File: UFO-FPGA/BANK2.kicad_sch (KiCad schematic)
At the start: 11 parts, among them U1 ICE40HX8K-BG121

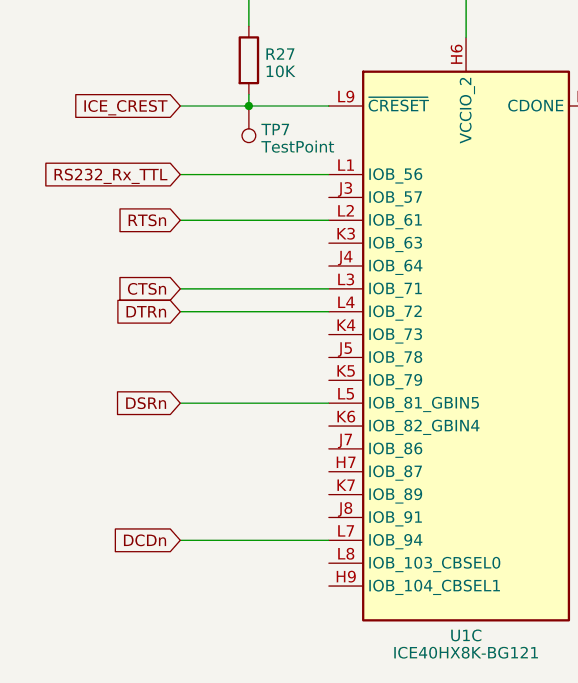
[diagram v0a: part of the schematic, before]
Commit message: Opamp gemaakt van de ADC
Enkel nog begrijpen wat VDC is. Aan docent vragen?
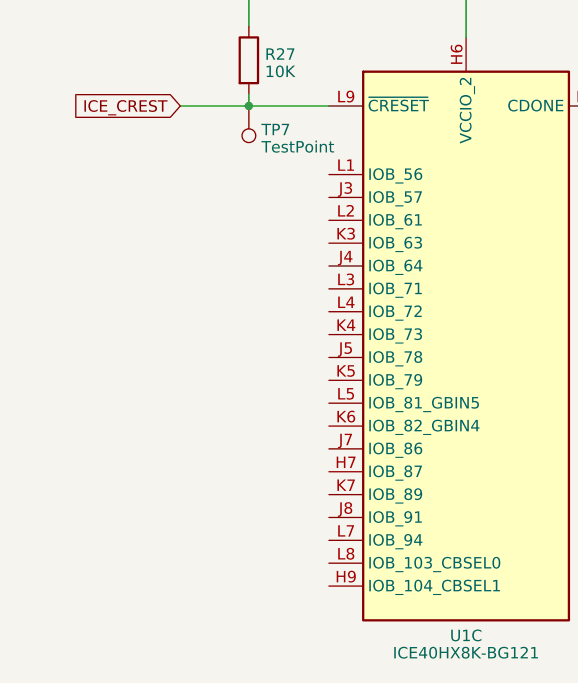
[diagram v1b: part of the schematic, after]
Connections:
- net CTSn: no longer names the net of U1.L3 (IOB_71)
- net DCDn: no longer names the net of U1.L7 (IOB_94)
- net DSRn: no longer names the net of U1.L5 (IOB_81_GBIN5)
- net DTRn: no longer names the net of U1.L4 (IOB_72)
- net RS232_Rx_TTL: no longer names the net of U1.L1 (IOB_56)
- net RTSn: no longer names the net of U1.L2 (IOB_61)
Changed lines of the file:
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@@
-    (stroke (width 0) (type default))
-  )
-  (wire (pts (xy 114.3 71.12) (xy 130.81 71.12))
     (stroke (width 0) (type default))
   )
@@
     (stroke (width 0) (type default))
   )
-  (wire (pts (xy 114.3 66.04) (xy 130.81 66.04))
-    (stroke (width 0) (type default))
-  )
-  (wire (pts (xy 114.3 106.68) (xy 130.81 106.68))
-    (stroke (width 0) (type default))
-  )
-  (wire (pts (xy 114.3 78.74) (xy 130.81 78.74))
-    (stroke (width 0) (type default))
-  )
   (wire (pts (xy 198.12 58.42) (xy 204.47 58.42))
-    (stroke (width 0) (type default))
-  )
-  (wire (pts (xy 114.3 91.44) (xy 130.81 91.44))
     (stroke (width 0) (type default))
   )
@@
   )
   (wire (pts (xy 146.05 38.1) (xy 146.05 50.8))
-    (stroke (width 0) (type default))
-  )
-  (wire (pts (xy 114.3 81.28) (xy 130.81 81.28))
     (stroke (width 0) (type default))
   )
@@
     (effects (font (size 1.27 1.27)) (justify left bottom))
   )
-  (global_label "RS232_Rx_TTL" (shape input) (at 114.3 66.04 180) (fields_autoplaced)
-    (effects (font (size 1.27 1.27)) (justify right))
-    (property "Intersheetrefs" "${INTERSHEET_REFS}" (at 98.0896 66.04 0)
-      (effects (font (size 1.27 1.27)) (justify right) hide)
-    )
-  )
-  (global_label "DTRn" (shape input) (at 114.3 81.28 180) (fields_autoplaced)
-    (effects (font (size 1.27 1.27)) (justify right))
-    (property "Intersheetrefs" "${INTERSHEET_REFS}" (at 106.7376 81.28 0)
-      (effects (font (size 1.27 1.27)) (justify right) hide)
-    )
-  )
   (global_label "ICE_CREST" (shape input) (at 114.3 58.42 180) (fields_autoplaced)
     (effects (font (size 1.27 1.27)) (justify right))
@@
       (effects (font (size 1.27 1.27)) (justify right) hide)
     )
-  )
-  (global_label "RTSn" (shape input) (at 114.3 71.12 180) (fields_autoplaced)
-    (effects (font (size 1.27 1.27)) (justify right))
-    (property "Intersheetrefs" "${INTERSHEET_REFS}" (at 106.7981 71.12 0)
-      (effects (font (size 1.27 1.27)) (justify right) hide)
-    )
-  )
-  (global_label "DSRn" (shape input) (at 114.3 91.44 180) (fields_autoplaced)
-    (effects (font (size 1.27 1.27)) (justify right))
-    (property "Intersheetrefs" "${INTERSHEET_REFS}" (at 106.4957 91.44 0)
-      (effects (font (size 1.27 1.27)) (justify right) hide)
-    )
-  )
-  (global_label "CTSn" (shape input) (at 114.3 78.74 180) (fields_autoplaced)
-    (effects (font (size 1.27 1.27)) (justify right))
-    (property "Intersheetrefs" "${INTERSHEET_REFS}" (at 106.7981 78.74 0)
-      (effects (font (size 1.27 1.27)) (justify right) hide)
-    )
-  )
-  (global_label "DCDn" (shape input) (at 114.3 106.68 180) (fields_autoplaced)
-    (effects (font (size 1.27 1.27)) (justify right))
-    (property "Intersheetrefs" "${INTERSHEET_REFS}" (at 106.4352 106.68 0)
-      (effects (font (size 1.27 1.27)) (justify right) hide)
-    )

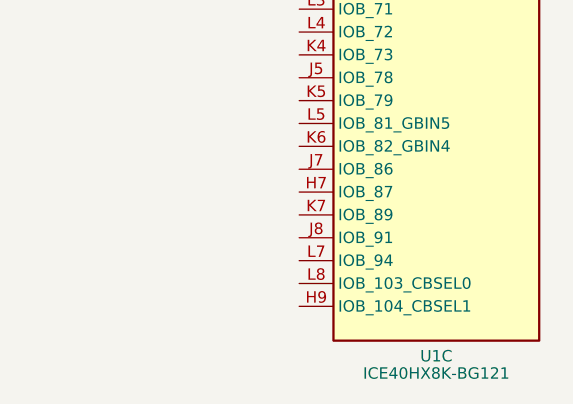
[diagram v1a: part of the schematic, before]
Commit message: Arduino PCB
Added Arduino PCB format
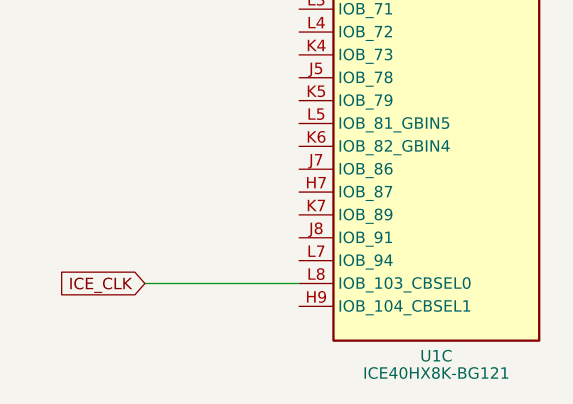
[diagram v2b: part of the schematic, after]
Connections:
- net ICE_CLK: now reaches U1.L8 (IOB_103_CBSEL0)
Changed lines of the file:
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@@
+    (stroke (width 0) (type default))
+  )
+  (wire (pts (xy 113.665 109.22) (xy 130.81 109.22))
     (stroke (width 0) (type default))
   )
@@
     (effects (font (size 1.27 1.27)) (justify left bottom))
   )
+  (global_label "ICE_CLK" (shape input) (at 113.665 109.22 180) (fields_autoplaced)
+    (effects (font (size 1.27 1.27)) (justify right))
+    (property "Intersheetrefs" "${INTERSHEET_REFS}" (at 103.1997 109.22 0)
+      (effects (font (size 1.27 1.27)) (justify right) hide)
+    )
+  )
   (global_label "ICE_CREST" (shape input) (at 114.3 58.42 180) (fields_autoplaced)

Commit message: pins and USB
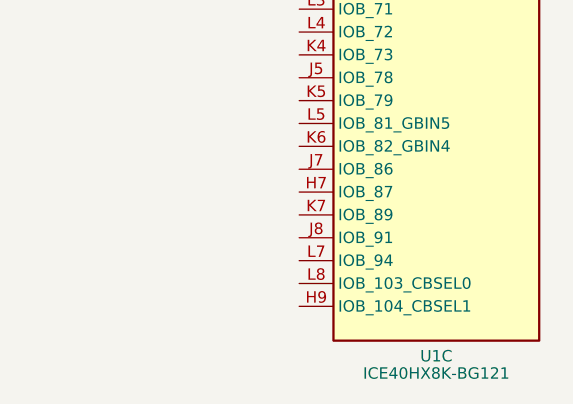
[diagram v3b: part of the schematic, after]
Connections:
- net ICE_CLK: no longer names the net of U1.L8 (IOB_103_CBSEL0)
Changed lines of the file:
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@@
-    (stroke (width 0) (type default))
-  )
-  (wire (pts (xy 113.665 109.22) (xy 130.81 109.22))
     (stroke (width 0) (type default))
   )
@@
     (effects (font (size 1.27 1.27)) (justify left bottom))
   )
-  (global_label "ICE_CLK" (shape input) (at 113.665 109.22 180) (fields_autoplaced)
-    (effects (font (size 1.27 1.27)) (justify right))
-    (property "Intersheetrefs" "${INTERSHEET_REFS}" (at 103.1997 109.22 0)
-      (effects (font (size 1.27 1.27)) (justify right) hide)
-    )
-  )
   (global_label "ICE_CREST" (shape input) (at 114.3 58.42 180) (fields_autoplaced)

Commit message: IO and power
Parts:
- removed C17 (x3): 100nF, symbol Device:C
- removed R25: 649, symbol Device:R
- removed R25: 1, symbol Device:R
- added C17 (x3): 100nF, symbol Device:C
- added R25: 649, symbol Device:R
- added R25: 1, symbol Device:R
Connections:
- net +1V2: now also R25.1
- net GND: now also C17.2, C17.2, C17.2
- net ICE_CDONE: now also R25.2
- net VCCIO_2: now also C17.1, C17.1, C17.1, R25.1, R25.2
- net RS232_Rx_TTL: now reaches U1.L1 (IOB_56)
- net RTSn: now reaches U1.L2 (IOB_61)
- net CTSn: now reaches U1.L3 (IOB_71)
- net DTRn: now reaches U1.L4 (IOB_72)
- net DSRn: now reaches U1.L5 (IOB_81_GBIN5)
- net DCDn: now reaches U1.L7 (IOB_94)

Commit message: Revision
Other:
- company: (none) -> Universal-Field-Objects
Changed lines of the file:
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@@
   (paper "A4")
   (title_block
-    (date "2023-04-22")
-    (rev "V0.1")
+    (date "2023-04-25")
+    (rev "V0.5")
+    (company "Universal-Field-Objects")
   )
   (junction (at 150.495 52.07) (diameter 0) (color 0 0 0 0)

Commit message: footprints and PCB
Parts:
- D2: footprint (none) -> LED_SMD:LED_0805_2012Metric_Pad1.15x1.40mm_HandSolder
- R25, R27: footprint (none) -> Resistor_SMD:R_0805_2012Metric_Pad1.20x1.40mm_HandSolder
- TP7, TP8: footprint (none) -> TestPoint:TestPoint_Keystone_5000-5004_Miniature
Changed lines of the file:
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@@
       (effects (font (size 1.27 1.27)) (justify right))
     )
-    (property "Footprint" "" (at 178.435 78.74 0)
+    (property "Footprint" "LED_SMD:LED_0805_2012Metric_Pad1.15x1.40mm_HandSolder" (at 178.435 78.74 0)
       (effects (font (size 1.27 1.27)) hide)
     )
@@
       (effects (font (size 1.27 1.27)))
     )
-    (property "Footprint" "" (at 188.595 50.292 90)
+    (property "Footprint" "Resistor_SMD:R_0805_2012Metric_Pad1.20x1.40mm_HandSolder" (at 188.595 50.292 90)
       (effects (font (size 1.27 1.27)) hide)
     )
@@
       (effects (font (size 1.27 1.27)) (justify left))
     )
-    (property "Footprint" "" (at 100.457 67.31 90)
+    (property "Footprint" "Resistor_SMD:R_0805_2012Metric_Pad1.20x1.40mm_HandSolder" (at 100.457 67.31 90)
       (effects (font (size 1.27 1.27)) hide)
     )
@@
       (effects (font (size 1.27 1.27)) (justify left))
     )
-    (property "Footprint" "" (at 179.705 52.07 0)
+    (property "Footprint" "TestPoint:TestPoint_Keystone_5000-5004_Miniature" (at 179.705 52.07 0)
       (effects (font (size 1.27 1.27)) hide)
     )
@@
       (effects (font (size 1.27 1.27)) (justify right))
     )
-    (property "Footprint" "" (at 97.155 72.39 0)
-      (effects (font (size 1.27 1.27)) hide)
-    )
+    (property "Footprint" "TestPoint:TestPoint_Keystone_5000-5004_Miniature" (at 97.155 72.39 0)
+      (effects (font (size 1.27 1.27)) hide)
+    )

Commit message: footprint
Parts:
- C17, C18: footprint (none) -> Capacitor_SMD:C_0805_2012Metric_Pad1.18x1.45mm_HandSolder
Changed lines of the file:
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@@
       (effects (font (size 1.27 1.27)) (justify left))
     )
-    (property "Footprint" "" (at 149.5298 59.69 0)
+    (property "Footprint" "Capacitor_SMD:C_0805_2012Metric_Pad1.18x1.45mm_HandSolder" (at 149.5298 59.69 0)
       (effects (font (size 1.27 1.27)) hide)
     )
@@
       (effects (font (size 1.27 1.27)) (justify left))
     )
-    (property "Footprint" "" (at 172.3898 59.69 0)
+    (property "Footprint" "Capacitor_SMD:C_0805_2012Metric_Pad1.18x1.45mm_HandSolder" (at 172.3898 59.69 0)
       (effects (font (size 1.27 1.27)) hide)
     )
@@
       (effects (font (size 1.27 1.27)) (justify left))
     )
-    (property "Footprint" "" (at 138.0998 59.69 0)
+    (property "Footprint" "Capacitor_SMD:C_0805_2012Metric_Pad1.18x1.45mm_HandSolder" (at 138.0998 59.69 0)
       (effects (font (size 1.27 1.27)) hide)
     )
@@
       (effects (font (size 1.27 1.27)) (justify left))
     )
-    (property "Footprint" "" (at 160.9598 59.69 0)
-      (effects (font (size 1.27 1.27)) hide)
-    )
+    (property "Footprint" "Capacitor_SMD:C_0805_2012Metric_Pad1.18x1.45mm_HandSolder" (at 160.9598 59.69 0)
+      (effects (font (size 1.27 1.27)) hide)
+    )

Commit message: Footprints and values
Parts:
- added R25: 130R, Resistor_SMD:R_0805_2012Metric_Pad1.20x1.40mm_HandSolder, symbol Device:R
- R25: value 649 -> 510R; footprint (none) -> Resistor_SMD:R_0805_2012Metric_Pad1.20x1.40mm_HandSolder
- R25: value 1 -> 1R
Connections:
- net ICE_CDONE: now also R25.2; no longer R25.2
- new net: R25.1, R25.2
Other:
- moved on the sheet: R25
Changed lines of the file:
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@@
+    (stroke (width 0) (type default))
+  )
+  (wire (pts (xy 178.435 70.485) (xy 178.435 72.39))
     (stroke (width 0) (type default))
   )
@@
     (stroke (width 0) (type default))
   )
+  (wire (pts (xy 94.615 85.09) (xy 111.125 85.09))
+    (stroke (width 0) (type default))
+  )
+  (wire (pts (xy 141.605 72.39) (xy 178.435 72.39))
+    (stroke (width 0) (type default))
+  )
+  (wire (pts (xy 161.925 52.07) (xy 173.355 52.07))
+    (stroke (width 0) (type default))
+  )
+  (wire (pts (xy 126.365 52.07) (xy 126.365 64.77))
+    (stroke (width 0) (type default))
+  )
+  (wire (pts (xy 192.405 41.91) (xy 192.405 52.07))
+    (stroke (width 0) (type default))
+  )
+  (wire (pts (xy 174.625 52.07) (xy 173.355 52.07))
+    (stroke (width 0) (type default))
+  )
+  (wire (pts (xy 139.065 52.07) (xy 126.365 52.07))
+    (stroke (width 0) (type default))
+  )
+  (wire (pts (xy 94.615 105.41) (xy 111.125 105.41))
+    (stroke (width 0) (type default))
+  )
+  (wire (pts (xy 161.925 52.07) (xy 150.495 52.07))
+    (stroke (width 0) (type default))
+  )
+  (wire (pts (xy 94.615 120.65) (xy 111.125 120.65))
+    (stroke (width 0) (type default))
+  )
+  (wire (pts (xy 94.615 72.39) (xy 102.235 72.39))
+    (stroke (width 0) (type default))
+  )
+  (wire (pts (xy 161.925 59.69) (xy 173.355 59.69))
+    (stroke (width 0) (type default))
+  )
+  (wire (pts (xy 150.495 52.07) (xy 139.065 52.07))
+    (stroke (width 0) (type default))
+  )
+  (wire (pts (xy 178.435 60.325) (xy 178.435 62.865))
+    (stroke (width 0) (type default))
+  )
+  (wire (pts (xy 102.235 72.39) (xy 111.125 72.39))
+    (stroke (width 0) (type default))
+  )
+  (wire (pts (xy 94.615 92.71) (xy 111.125 92.71))
+    (stroke (width 0) (type default))
+  )
+  (wire (pts (xy 150.495 59.69) (xy 139.065 59.69))
+    (stroke (width 0) (type default))
+  )
   (wire (pts (xy 174.625 52.07) (xy 178.435 52.07))
     (stroke (width 0) (type default))
   )
-  (wire (pts (xy 94.615 85.09) (xy 111.125 85.09))
-    (stroke (width 0) (type default))
-  )
-  (wire (pts (xy 141.605 72.39) (xy 178.435 72.39))
-    (stroke (width 0) (type default))
-  )
-  (wire (pts (xy 161.925 52.07) (xy 173.355 52.07))
-    (stroke (width 0) (type default))
-  )
-  (wire (pts (xy 126.365 52.07) (xy 126.365 64.77))
-    (stroke (width 0) (type default))
-  )
-  (wire (pts (xy 192.405 41.91) (xy 192.405 52.07))
-    (stroke (width 0) (type default))
-  )
-  (wire (pts (xy 174.625 52.07) (xy 173.355 52.07))
-    (stroke (width 0) (type default))
-  )
-  (wire (pts (xy 139.065 52.07) (xy 126.365 52.07))
-    (stroke (width 0) (type default))
-  )
-  (wire (pts (xy 94.615 105.41) (xy 111.125 105.41))
-    (stroke (width 0) (type default))
-  )
-  (wire (pts (xy 161.925 52.07) (xy 150.495 52.07))
-    (stroke (width 0) (type default))
-  )
-  (wire (pts (xy 178.435 64.77) (xy 178.435 72.39))
-    (stroke (width 0) (type default))
-  )
-  (wire (pts (xy 94.615 120.65) (xy 111.125 120.65))
-    (stroke (width 0) (type default))
-  )
-  (wire (pts (xy 94.615 72.39) (xy 102.235 72.39))
-    (stroke (width 0) (type default))
-  )
-  (wire (pts (xy 161.925 59.69) (xy 173.355 59.69))
-    (stroke (width 0) (type default))
-  )
-  (wire (pts (xy 150.495 52.07) (xy 139.065 52.07))
-    (stroke (width 0) (type default))
-  )
-  (wire (pts (xy 102.235 72.39) (xy 111.125 72.39))
-    (stroke (width 0) (type default))
-  )
-  (wire (pts (xy 94.615 92.71) (xy 111.125 92.71))
-    (stroke (width 0) (type default))
-  )
-  (wire (pts (xy 150.495 59.69) (xy 139.065 59.69))
+  (wire (pts (xy 178.435 72.39) (xy 178.435 74.93))
     (stroke (width 0) (type default))
   )
@@
     (stroke (width 0) (type default))
   )
-  (wire (pts (xy 178.435 72.39) (xy 178.435 74.93))
-    (stroke (width 0) (type default))
-  )
-  (wire (pts (xy 178.435 52.07) (xy 178.435 57.15))
-    (stroke (width 0) (type default))
-  )
   (wire (pts (xy 178.435 72.39) (xy 184.785 72.39))
+    (stroke (width 0) (type default))
+  )
+  (wire (pts (xy 178.435 52.07) (xy 178.435 52.705))
     (stroke (width 0) (type default))
   )
@@
     )
   )
-  (symbol (lib_id "Device:R") (at 178.435 60.96 0) (unit 1)
+  (symbol (lib_id "Device:R") (at 178.435 56.515 0) (unit 1)
     (in_bom yes) (on_board yes) (dnp no)
-    (property "Reference" "R25" (at 182.4609 60.96 90)
-      (effects (font (size 1.27 1.27)))
-    )
-    (property "Value" "649" (at 180.5399 60.96 90)
-      (effects (font (size 1.27 1.27)))
-    )
-    (property "Footprint" "" (at 176.657 60.96 90)
-      (effects (font (size 1.27 1.27)) hide)
-    )
-    (property "Datasheet" "~" (at 178.435 60.96 0)
+    (property "Reference" "R25" (at 182.4609 56.515 90)
+      (effects (font (size 1.27 1.27)))
+    )
+    (property "Value" "510R" (at 180.5399 56.515 90)
+      (effects (font (size 1.27 1.27)))
+    )
+    (property "Footprint" "Resistor_SMD:R_0805_2012Metric_Pad1.20x1.40mm_HandSolder" (at 176.657 56.515 90)
+      (effects (font (size 1.27 1.27)) hide)
+    )
+    (property "Datasheet" "~" (at 178.435 56.515 0)
       (effects (font (size 1.27 1.27)) hide)
     )
@@
         (path "/b3168f6a-c732-41d3-aeeb-d97dd2f1bb65/6f7e0d88-d92b-4c4f-9dc8-64721cd46d41"
           (reference "#PWR029") (unit 1)
+        )
+      )
+    )
+  )
+  (symbol (lib_id "Device:R") (at 178.435 66.675 0) (unit 1)
+    (in_bom yes) (on_board yes) (dnp no)
+    (property "Reference" "R25" (at 182.4609 66.675 90)
+      (effects (font (size 1.27 1.27)))
+    )
+    (property "Value" "130R" (at 180.5399 66.675 90)
+      (effects (font (size 1.27 1.27)))
+    )
+    (property "Footprint" "Resistor_SMD:R_0805_2012Metric_Pad1.20x1.40mm_HandSolder" (at 176.657 66.675 90)
+      (effects (font (size 1.27 1.27)) hide)
+    )
+    (property "Datasheet" "~" (at 178.435 66.675 0)
+      (effects (font (size 1.27 1.27)) hide)
+    )
+    (pin "1")
+    (pin "2")
+    (instances
+      (project "UFO-FPGA"
+        (path "/b3168f6a-c732-41d3-aeeb-d97dd2f1bb65/a9a0295d-b075-4952-a5ba-04debc5f691c"
+          (reference "R25") (unit 1)
+        )
+        (path "/b3168f6a-c732-41d3-aeeb-d97dd2f1bb65/6f7e0d88-d92b-4c4f-9dc8-64721cd46d41"
+          (reference "R56") (unit 1)
         )
       )
@@
       (effects (font (size 1.27 1.27)))
     )
-    (property "Value" "1" (at 188.595 54.1749 90)
-      (effects (font (size 1.27 1.27)))
-    )
+    (property "Value" "1R" (at 188.595 54.1749 90)
+      (effects (font (size 1.27 1.27)))
+    )
